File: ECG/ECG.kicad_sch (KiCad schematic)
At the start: 52 parts, among them J1 Conn_01x03, J2 Conn_01x03, J3 Conn_01x15, J4 Conn_01x15, J5 Conn_01x02, Q1 DMG2301L, Q2 T2N7002AK, Q3 T2N7002AK, Q4 T2N7002AK, Q5 T2N7002AK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

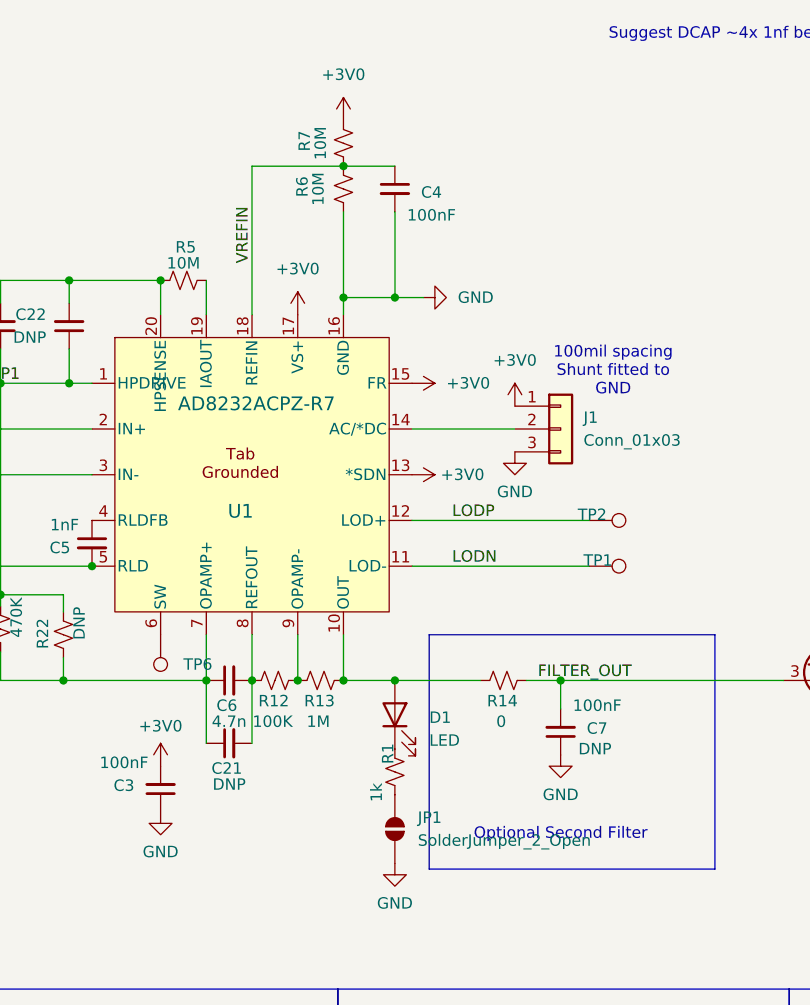
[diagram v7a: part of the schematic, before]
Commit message: Vref, add TPs
Added R17, TP7, TP8
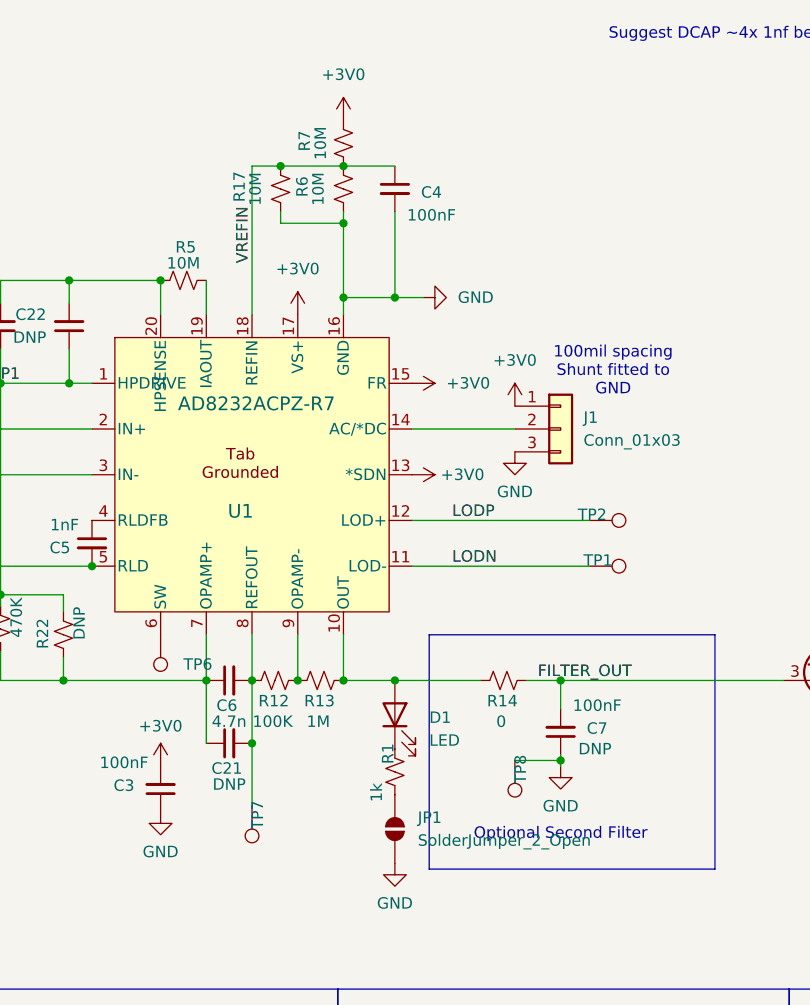
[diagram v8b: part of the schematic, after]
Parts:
- added R17: 10M, Resistor_SMD:R_0603_1608Metric, symbol Device:R_Small_US
- added TP7, TP8: TestPoint, TestPoint:TestPoint_Keystone_5000-5004_Miniature, symbol Connector:TestPoint
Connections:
- net GND: now also R17.2, TP8.1
- net VREFIN: now also R17.1
- net at C21.2, C6.2, R12.1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: now also TP7.1
